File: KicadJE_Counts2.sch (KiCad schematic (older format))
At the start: 84 parts, among them J301 Doepfer connector, J302 In_1, J303 In 2, J304 Out 1, J305 Out 2, J306 Out 1 Final, J307 Out 2 Final, U301 TL072, U302 TL072

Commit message: Update KicadJE_Counts2.sch
Dummy diode light
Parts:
- added D?: LED, AJ:LED_0805_2012Metric_Pad1.15x1.40mm_HandSolder, symbol Device:LED
- added R?: 10k, AJ:R_0805_AJ, symbol Device:R
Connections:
- net +12V: now also R?.2
- net GND: now also D?.1 (K)
- new net: D?.2 (A), R?.1
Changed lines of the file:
@@
 Text HLabel 3250 3500 2    50   Input ~ 0
 POT2_L
+$Comp
+L Device:LED D?
+U 1 1 5EC9B7FD
+P 3950 1400
+F 0 "D?" V 3989 1282 50  0000 R CNN
+F 1 "LED" V 3898 1282 50  0000 R CNN
+F 2 "AJ:LED_0805_2012Metric_Pad1.15x1.40mm_HandSolder" H 3950 1400 50  0001 C CNN
+F 3 "~" H 3950 1400 50  0001 C CNN
+	1    3950 1400
+	0    -1   -1   0
+$EndComp
+$Comp
+L Device:R R?
+U 1 1 5EC9D17F
+P 3950 1025
+AR Path="/5CF11B19/5EC9D17F" Ref="R?"  Part="1"
+AR Path="/5D4DB615/5EC9D17F" Ref="R?"  Part="1"
+AR Path="/5D60ED9A/5EC9D17F" Ref="R?"  Part="1"
+F 0 "R?" V 3950 1025 50  0000 C CNN
+F 1 "10k" V 3875 1000 50  0000 C CNN
+F 2 "AJ:R_0805_AJ" V 3880 1025 50  0001 C CNN
+F 3 "~" H 3950 1025 50  0001 C CNN
+	1    3950 1025
+	-1   0    0    1
+$EndComp
+Text GLabel 3950 825  1    50   Input ~ 0
++12V
+$Comp
+L power:GND #PWR?
+U 1 1 5EC9DA7F
+P 3950 1650
+AR Path="/5EC9DA7F" Ref="#PWR?"  Part="1"
+AR Path="/5D60ED9A/5EC9DA7F" Ref="#PWR?"  Part="1"
+F 0 "#PWR?" H 3950 1400 50  0001 C CNN
+F 1 "GND" H 3955 1477 50  0000 C CNN
+F 2 "" H 3950 1650 50  0001 C CNN
+F 3 "" H 3950 1650 50  0001 C CNN
+	1    3950 1650
+	1    0    0    -1
+$EndComp
+Wire Wire Line
+	3950 1650 3950 1550
+Wire Wire Line
+	3950 1250 3950 1175
+Wire Wire Line
+	3950 875  3950 825
 $EndSCHEMATC

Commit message: Update KicadJE_Counts2.sch
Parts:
- gave numbers to parts that had none: 2
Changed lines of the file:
@@
 POT2_L
 $Comp
-L Device:LED D?
+L Device:LED D318
 U 1 1 5EC9B7FD
 P 3950 1400
-F 0 "D?" V 3989 1282 50  0000 R CNN
+F 0 "D318" V 3989 1282 50  0000 R CNN
 F 1 "LED" V 3898 1282 50  0000 R CNN
 F 2 "AJ:LED_0805_2012Metric_Pad1.15x1.40mm_HandSolder" H 3950 1400 50  0001 C CNN
@@
 AR Path="/5CF11B19/5EC9D17F" Ref="R?"  Part="1"
 AR Path="/5D4DB615/5EC9D17F" Ref="R?"  Part="1"
-AR Path="/5D60ED9A/5EC9D17F" Ref="R?"  Part="1"
-F 0 "R?" V 3950 1025 50  0000 C CNN
+AR Path="/5D60ED9A/5EC9D17F" Ref="R335"  Part="1"
+F 0 "R335" V 3950 1025 50  0000 C CNN
 F 1 "10k" V 3875 1000 50  0000 C CNN
 F 2 "AJ:R_0805_AJ" V 3880 1025 50  0001 C CNN
@@
 P 3950 1650
 AR Path="/5EC9DA7F" Ref="#PWR?"  Part="1"
-AR Path="/5D60ED9A/5EC9DA7F" Ref="#PWR?"  Part="1"
-F 0 "#PWR?" H 3950 1400 50  0001 C CNN
+AR Path="/5D60ED9A/5EC9DA7F" Ref="#PWR0302"  Part="1"
+F 0 "#PWR0302" H 3950 1400 50  0001 C CNN
 F 1 "GND" H 3955 1477 50  0000 C CNN
 F 2 "" H 3950 1650 50  0001 C CNN

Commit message: Update KicadJE_Counts2.sch
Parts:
- removed D318: LED, AJ:LED_0805_2012Metric_Pad1.15x1.40mm_HandSolder, symbol Device:LED
- removed R335: 10k, AJ:R_0805_AJ, symbol Device:R
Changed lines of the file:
@@
 Text HLabel 3250 3500 2    50   Input ~ 0
 POT2_L
-$Comp
-L Device:LED D318
-U 1 1 5EC9B7FD
-P 3950 1400
-F 0 "D318" V 3989 1282 50  0000 R CNN
-F 1 "LED" V 3898 1282 50  0000 R CNN
-F 2 "AJ:LED_0805_2012Metric_Pad1.15x1.40mm_HandSolder" H 3950 1400 50  0001 C CNN
-F 3 "~" H 3950 1400 50  0001 C CNN
-	1    3950 1400
-	0    -1   -1   0
-$EndComp
-$Comp
-L Device:R R?
-U 1 1 5EC9D17F
-P 3950 1025
-AR Path="/5CF11B19/5EC9D17F" Ref="R?"  Part="1"
-AR Path="/5D4DB615/5EC9D17F" Ref="R?"  Part="1"
-AR Path="/5D60ED9A/5EC9D17F" Ref="R335"  Part="1"
-F 0 "R335" V 3950 1025 50  0000 C CNN
-F 1 "10k" V 3875 1000 50  0000 C CNN
-F 2 "AJ:R_0805_AJ" V 3880 1025 50  0001 C CNN
-F 3 "~" H 3950 1025 50  0001 C CNN
-	1    3950 1025
-	-1   0    0    1
-$EndComp
-Text GLabel 3950 825  1    50   Input ~ 0
-+12V
-$Comp
-L power:GND #PWR?
-U 1 1 5EC9DA7F
-P 3950 1650
-AR Path="/5EC9DA7F" Ref="#PWR?"  Part="1"
-AR Path="/5D60ED9A/5EC9DA7F" Ref="#PWR0302"  Part="1"
-F 0 "#PWR0302" H 3950 1400 50  0001 C CNN
-F 1 "GND" H 3955 1477 50  0000 C CNN
-F 2 "" H 3950 1650 50  0001 C CNN
-F 3 "" H 3950 1650 50  0001 C CNN
-	1    3950 1650
-	1    0    0    -1
-$EndComp
-Wire Wire Line
-	3950 1650 3950 1550
-Wire Wire Line
-	3950 1250 3950 1175
-Wire Wire Line
-	3950 875  3950 825
 $EndSCHEMATC

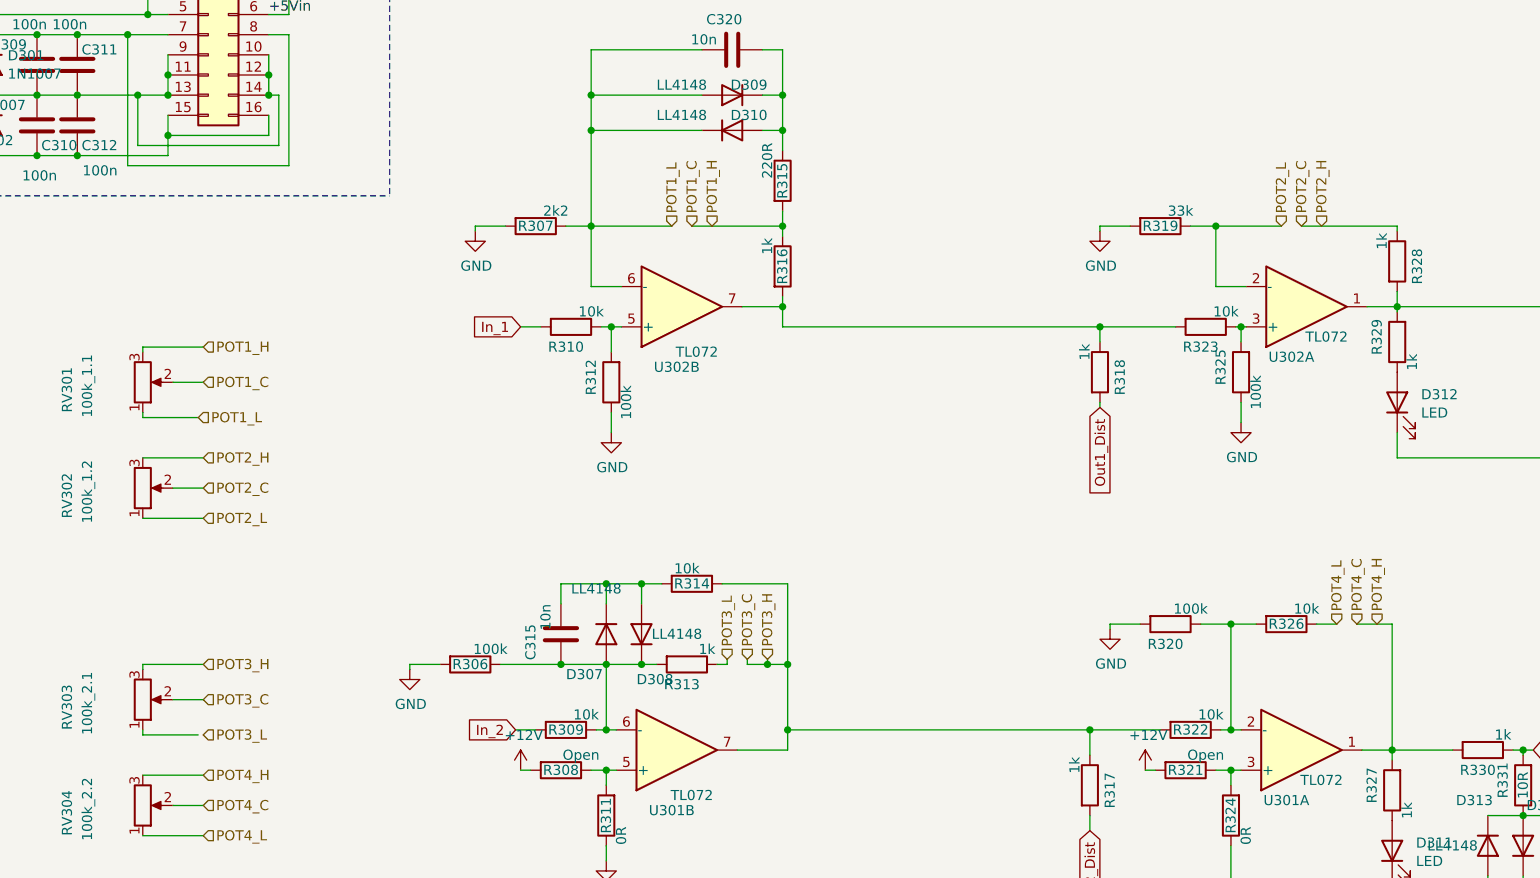
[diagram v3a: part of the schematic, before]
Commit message: Update KicadJE_Counts2.sch
conn pots
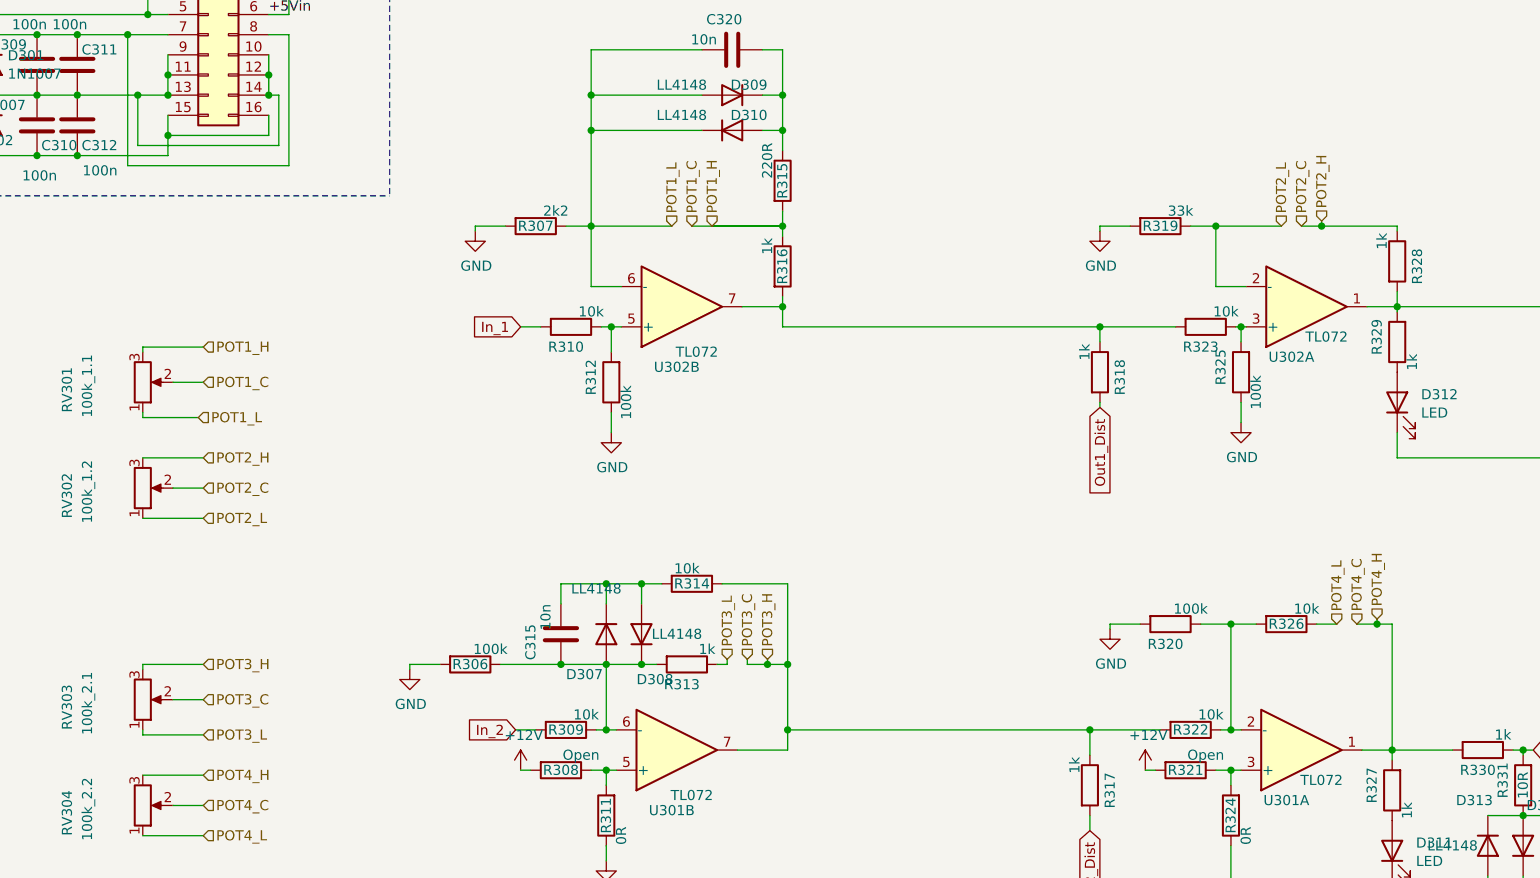
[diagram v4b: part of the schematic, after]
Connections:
- net POT3_L: now also RV303.1
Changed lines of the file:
@@
 Wire Wire Line
 	5800 4225 5850 4225
-Text HLabel 9075 4025 1    50   Input ~ 0
+Text HLabel 9075 4000 1    50   Input ~ 0
 POT4_H
 Text HLabel 8975 4025 1    50   Input ~ 0
@@
 	9750 4650 9800 4650
 Wire Wire Line
-	8975 4025 9150 4025
+	8975 4025 9075 4025
 Wire Wire Line
 	8875 4025 8775 4025
@@
 Wire Wire Line
 	5575 2050 5175 2050
-Wire Wire Line
-	5675 2050 6125 2050
-Text HLabel 8800 2050 1    50   Input ~ 0
+Text HLabel 8800 2025 1    50   Input ~ 0
 POT2_H
 Text HLabel 8700 2050 1    50   Input ~ 0
@@
 Wire Wire Line
 	8600 2050 8275 2050
-Wire Wire Line
-	8700 2050 9175 2050
 $Comp
 L Device:R R?
@@
 	2950 5075 3250 5075
 Wire Wire Line
-	3225 4575 2950 4575
-Wire Wire Line
 	2950 4575 2950 4550
 Wire Wire Line
@@
 Text HLabel 3250 3500 2    50   Input ~ 0
 POT2_L
+Wire Wire Line
+	2950 4575 3250 4575
+Wire Wire Line
+	5775 2050 6125 2050
+Wire Wire Line
+	5675 2050 6125 2050
+Wire Wire Line
+	8700 2050 8800 2050
+Wire Wire Line
+	8800 2025 8800 2050
+Connection ~ 8800 2050
+Wire Wire Line
+	8800 2050 9175 2050
+Wire Wire Line
+	9075 4000 9075 4025
+Connection ~ 9075 4025
+Wire Wire Line
+	9075 4025 9150 4025
 $EndSCHEMATC

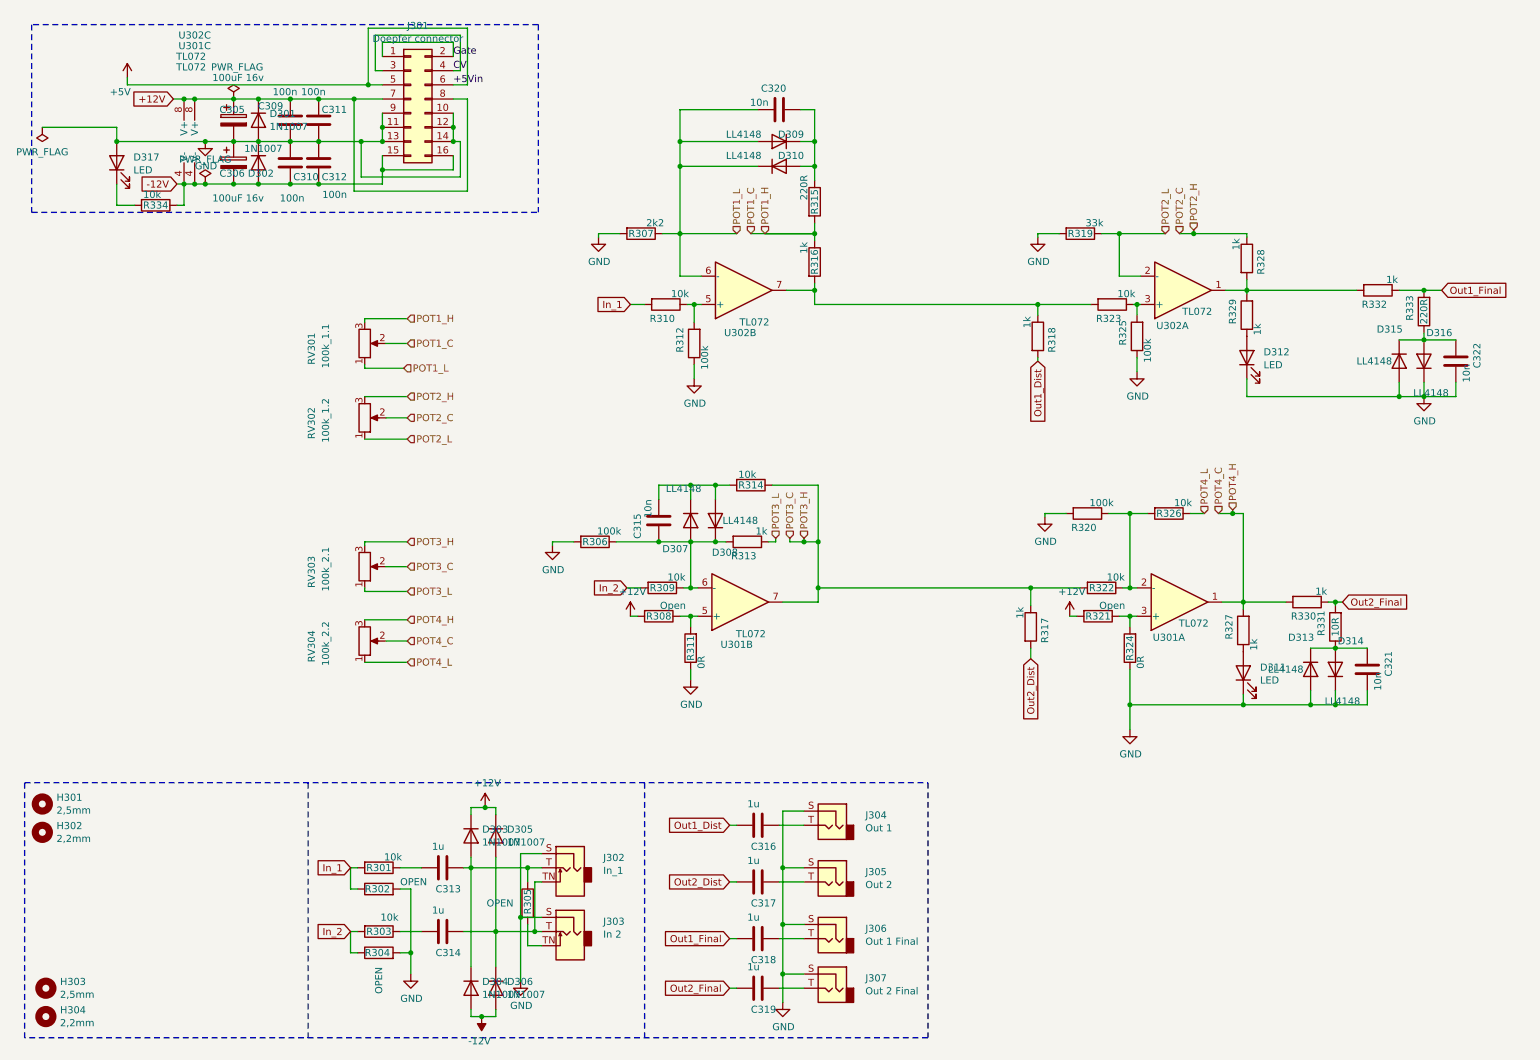
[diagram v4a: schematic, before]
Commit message: Changed label types for POT's
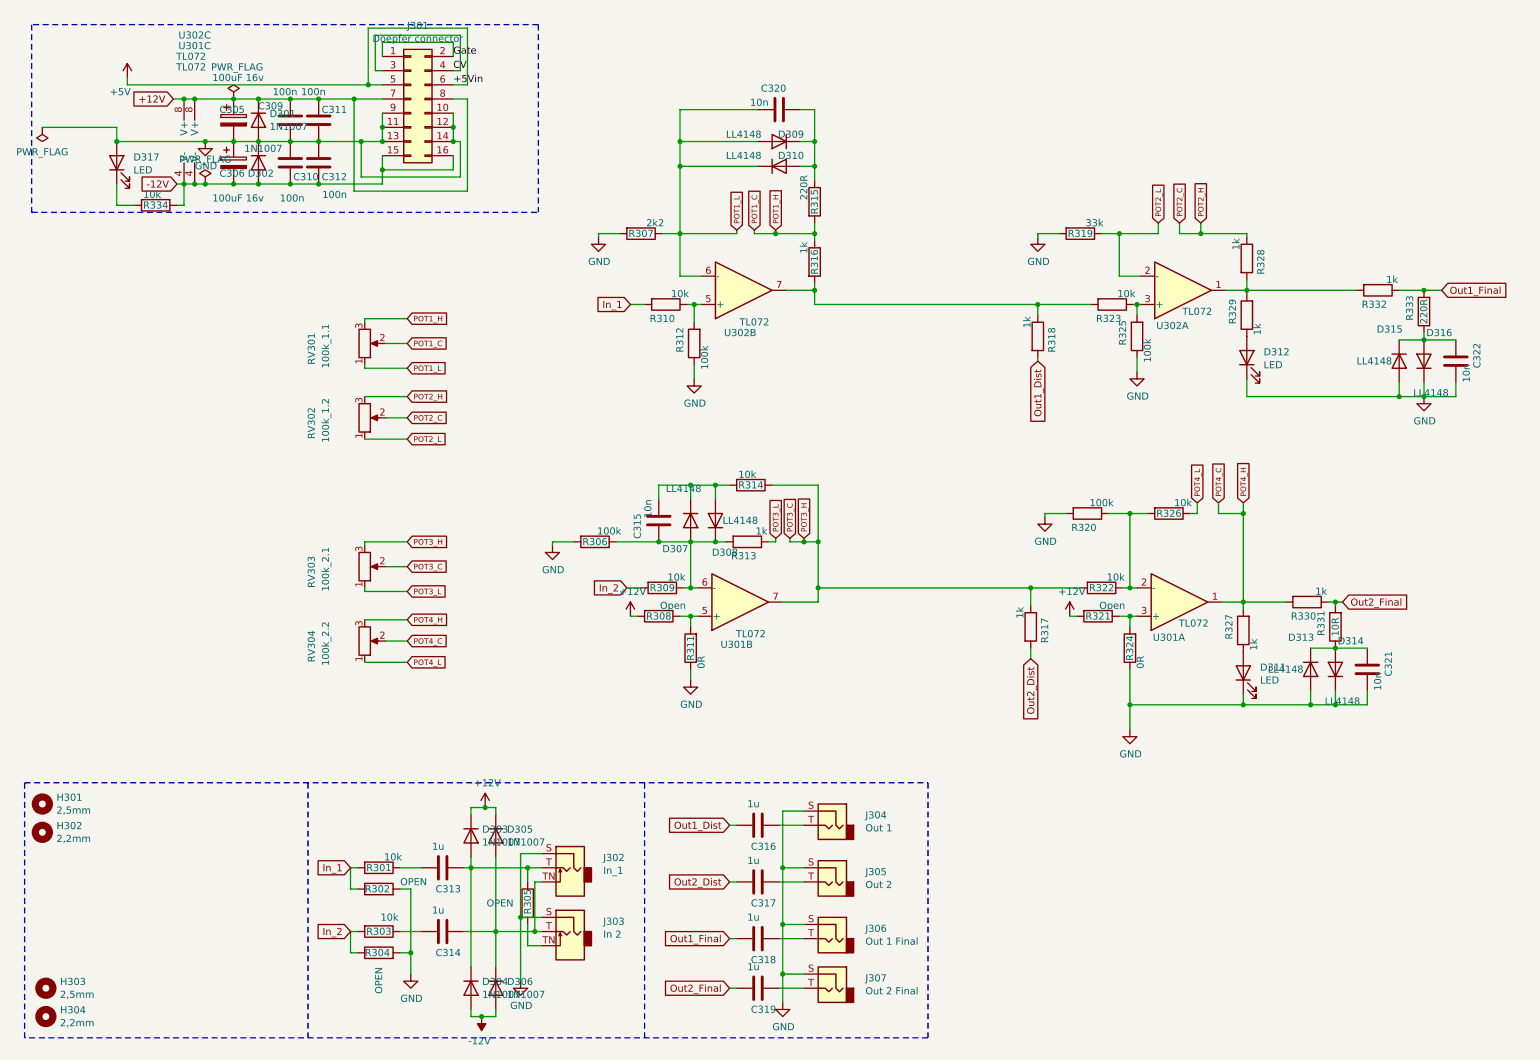
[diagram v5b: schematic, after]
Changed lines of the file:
@@
 	5175 2350 5175 2050
-Wire Wire Line
-	6125 2050 6125 2100
 Wire Wire Line
 	6125 2450 5925 2450
@@
 Wire Notes Line
 	4925 5925 4925 7725
-Text HLabel 6050 4200 1    50   Input ~ 0
-POT3_H
-Text HLabel 5950 4200 1    50   Input ~ 0
-POT3_C
-Text HLabel 5850 4200 1    50   Input ~ 0
-POT3_L
 $Comp
 L Diode:LL4148 D?
@@
 Wire Wire Line
 	5800 4225 5850 4225
-Text HLabel 9075 4000 1    50   Input ~ 0
-POT4_H
-Text HLabel 8975 4025 1    50   Input ~ 0
-POT4_C
-Text HLabel 8875 4025 1    50   Input ~ 0
-POT4_L
 Wire Wire Line
 	9150 4025 9150 4650
@@
 	9750 4650 9800 4650
 Wire Wire Line
-	8975 4025 9075 4025
-Wire Wire Line
-	8875 4025 8775 4025
-Text HLabel 5775 2050 1    50   Input ~ 0
-POT1_H
-Text HLabel 5675 2050 1    50   Input ~ 0
-POT1_C
-Text HLabel 5575 2050 1    50   Input ~ 0
-POT1_L
-Wire Wire Line
 	5575 2050 5175 2050
-Text HLabel 8800 2025 1    50   Input ~ 0
-POT2_H
-Text HLabel 8700 2050 1    50   Input ~ 0
-POT2_C
-Text HLabel 8600 2050 1    50   Input ~ 0
-POT2_L
-Wire Wire Line
-	8600 2050 8275 2050
 $Comp
 L Device:R R?
@@
 Wire Wire Line
 	8150 2050 8275 2050
-Connection ~ 8275 2050
 $Comp
 L power:GND #PWR?
@@
 Wire Wire Line
 	6125 1575 6125 1675
-Connection ~ 6125 2050
 Wire Wire Line
 	5725 1175 5175 1175
@@
 	1    0    0    -1
 $EndComp
-Wire Wire Line
-	6125 1975 6125 2050
 $Comp
 L Diode:LL4148 D?
@@
 Wire Notes Line
 	600  1900 4175 1900
-Text HLabel 3250 4225 2    50   Input ~ 0
-POT3_H
-Text HLabel 3250 4400 2    50   Input ~ 0
-POT3_C
-Text HLabel 3250 4575 2    50   Input ~ 0
-POT3_L
-Text HLabel 3250 4775 2    50   Input ~ 0
-POT4_H
-Text HLabel 3250 4925 2    50   Input ~ 0
-POT4_C
-Text HLabel 3250 5075 2    50   Input ~ 0
-POT4_L
 $Comp
 L Device:R_POT RV?
@@
 	2950 3500 3250 3500
 Wire Wire Line
-	3225 3000 2950 3000
-Wire Wire Line
 	2950 3000 2950 2975
-Wire Wire Line
-	2950 2675 2950 2650
-Wire Wire Line
-	2950 2650 3250 2650
 Wire Wire Line
 	3100 2825 3250 2825
@@
 Wire Wire Line
 	1675 1850 1675 1700
-Text HLabel 3250 2650 2    50   Input ~ 0
+Wire Wire Line
+	2950 4575 3250 4575
+Wire Wire Line
+	3250 2650 2950 2650
+Wire Wire Line
+	2950 2650 2950 2675
+Wire Wire Line
+	6125 1975 6125 2050
+Wire Wire Line
+	5850 2025 5850 2050
+Wire Wire Line
+	5850 2050 6125 2050
+Connection ~ 6125 2050
+Wire Wire Line
+	6125 2050 6125 2100
+Connection ~ 5850 2050
+Wire Wire Line
+	5700 2050 5850 2050
+Wire Wire Line
+	5700 2050 5700 2025
+Wire Wire Line
+	5575 2050 5575 2025
+Text GLabel 5575 2025 1    39   Input ~ 0
+POT1_L
+Text GLabel 5700 2025 1    39   Input ~ 0
+POT1_C
+Text GLabel 5850 2025 1    39   Input ~ 0
 POT1_H
-Text HLabel 3250 2825 2    50   Input ~ 0
+Text GLabel 3250 3000 2    39   Input ~ 0
+POT1_L
+Text GLabel 3250 2825 2    39   Input ~ 0
 POT1_C
-Text HLabel 3225 3000 2    50   Input ~ 0
-POT1_L
-Text HLabel 3250 3200 2    50   Input ~ 0
+Text GLabel 3250 2650 2    39   Input ~ 0
+POT1_H
+Wire Wire Line
+	2950 3000 3250 3000
+Text GLabel 3250 3500 2    39   Input ~ 0
+POT2_L
+Text GLabel 3250 3350 2    39   Input ~ 0
+POT2_C
+Text GLabel 3250 3200 2    39   Input ~ 0
 POT2_H
-Text HLabel 3250 3350 2    50   Input ~ 0
+Text GLabel 8550 1975 1    39   Input ~ 0
+POT2_L
+Text GLabel 8700 1975 1    39   Input ~ 0
 POT2_C
-Text HLabel 3250 3500 2    50   Input ~ 0
-POT2_L
-Wire Wire Line
-	2950 4575 3250 4575
-Wire Wire Line
-	5775 2050 6125 2050
-Wire Wire Line
-	5675 2050 6125 2050
-Wire Wire Line
-	8700 2050 8800 2050
-Wire Wire Line
-	8800 2025 8800 2050
-Connection ~ 8800 2050
-Wire Wire Line
-	8800 2050 9175 2050
-Wire Wire Line
-	9075 4000 9075 4025
-Connection ~ 9075 4025
-Wire Wire Line
-	9075 4025 9150 4025
+Text GLabel 8850 1975 1    39   Input ~ 0
+POT2_H
+Wire Wire Line
+	8700 1975 8700 2050
+Wire Wire Line
+	8700 2050 8850 2050
+Wire Wire Line
+	8850 1975 8850 2050
+Connection ~ 8850 2050
+Wire Wire Line
+	8850 2050 9175 2050
+Wire Wire Line
+	8550 2050 8275 2050
+Connection ~ 8275 2050
+Wire Wire Line
+	8550 1975 8550 2050
+Text GLabel 3250 4575 2    39   Input ~ 0
+POT3_L
+Text GLabel 3250 4400 2    39   Input ~ 0
+POT3_C
+Text GLabel 3250 4225 2    39   Input ~ 0
+POT3_H
+Text GLabel 3250 5075 2    39   Input ~ 0
+POT4_L
+Text GLabel 3250 4925 2    39   Input ~ 0
+POT4_C
+Text GLabel 3250 4775 2    39   Input ~ 0
+POT4_H
+Text GLabel 5850 4200 1    39   Input ~ 0
+POT3_L
+Text GLabel 5950 4200 1    39   Input ~ 0
+POT3_C
+Text GLabel 6050 4200 1    39   Input ~ 0
+POT3_H
+Text GLabel 8825 3950 1    39   Input ~ 0
+POT4_L
+Text GLabel 8975 3950 1    39   Input ~ 0
+POT4_C
+Text GLabel 9150 3950 1    39   Input ~ 0
+POT4_H
+Wire Wire Line
+	8775 4025 8825 4025
+Wire Wire Line
+	8825 4025 8825 3950
+Wire Wire Line
+	8975 4025 9150 4025
+Wire Wire Line
+	8975 3950 8975 4025
+Wire Wire Line
+	9150 3950 9150 4025
+Connection ~ 9150 4025
 $EndSCHEMATC
